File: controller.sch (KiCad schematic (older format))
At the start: 25 parts, among them J1 Conn_01x04, J2 Conn_01x08, J3 Conn_01x16, SW1 SW_Push, U1 PRTR5V0U2X, U2 AT90USB1286-AU, Y1 16MHz

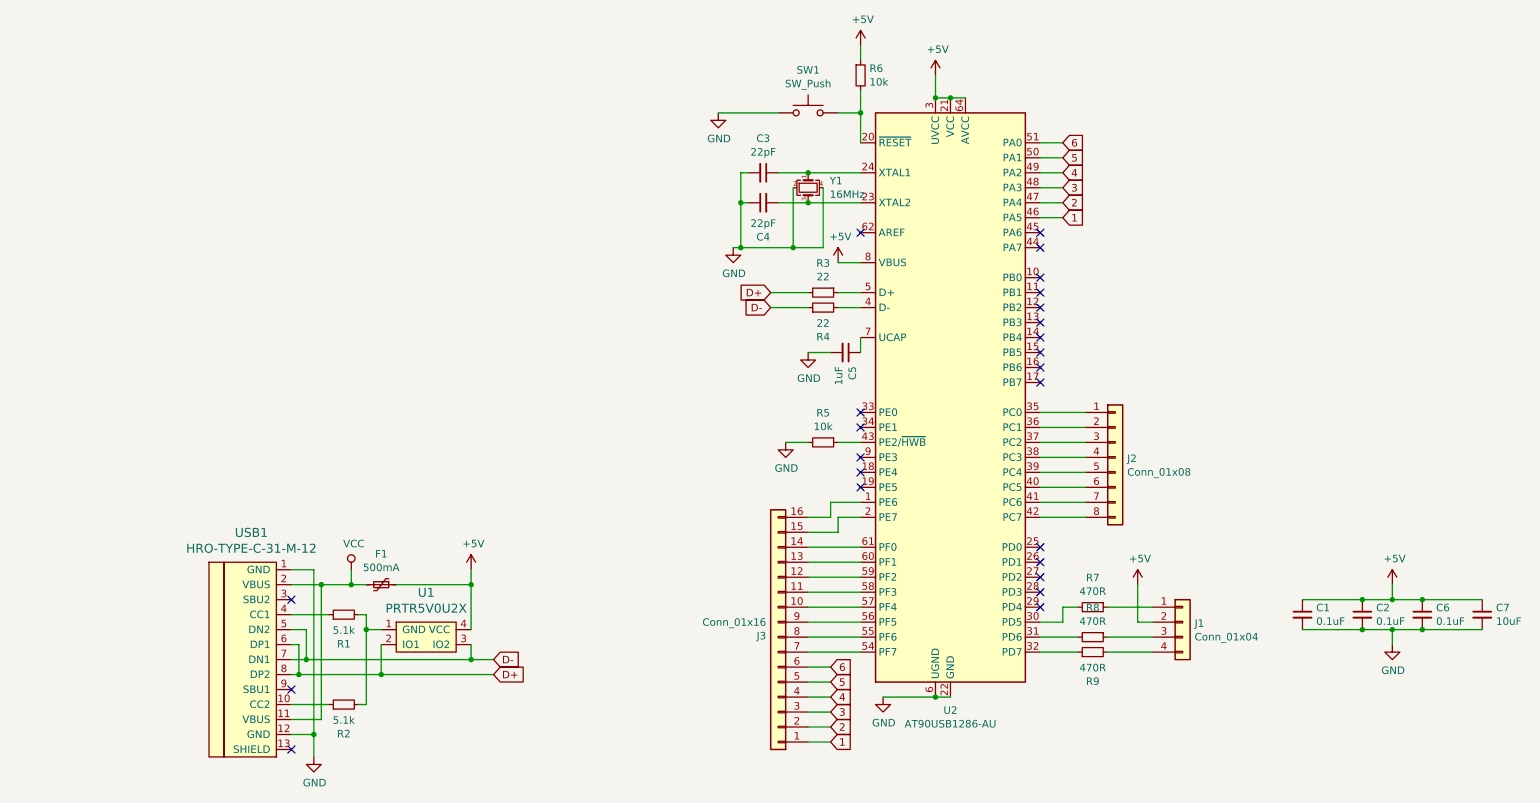
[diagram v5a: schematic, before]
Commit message: rev 2
Adjusted ucb-c location, fixed grounding error, changed some sizes to be more snug
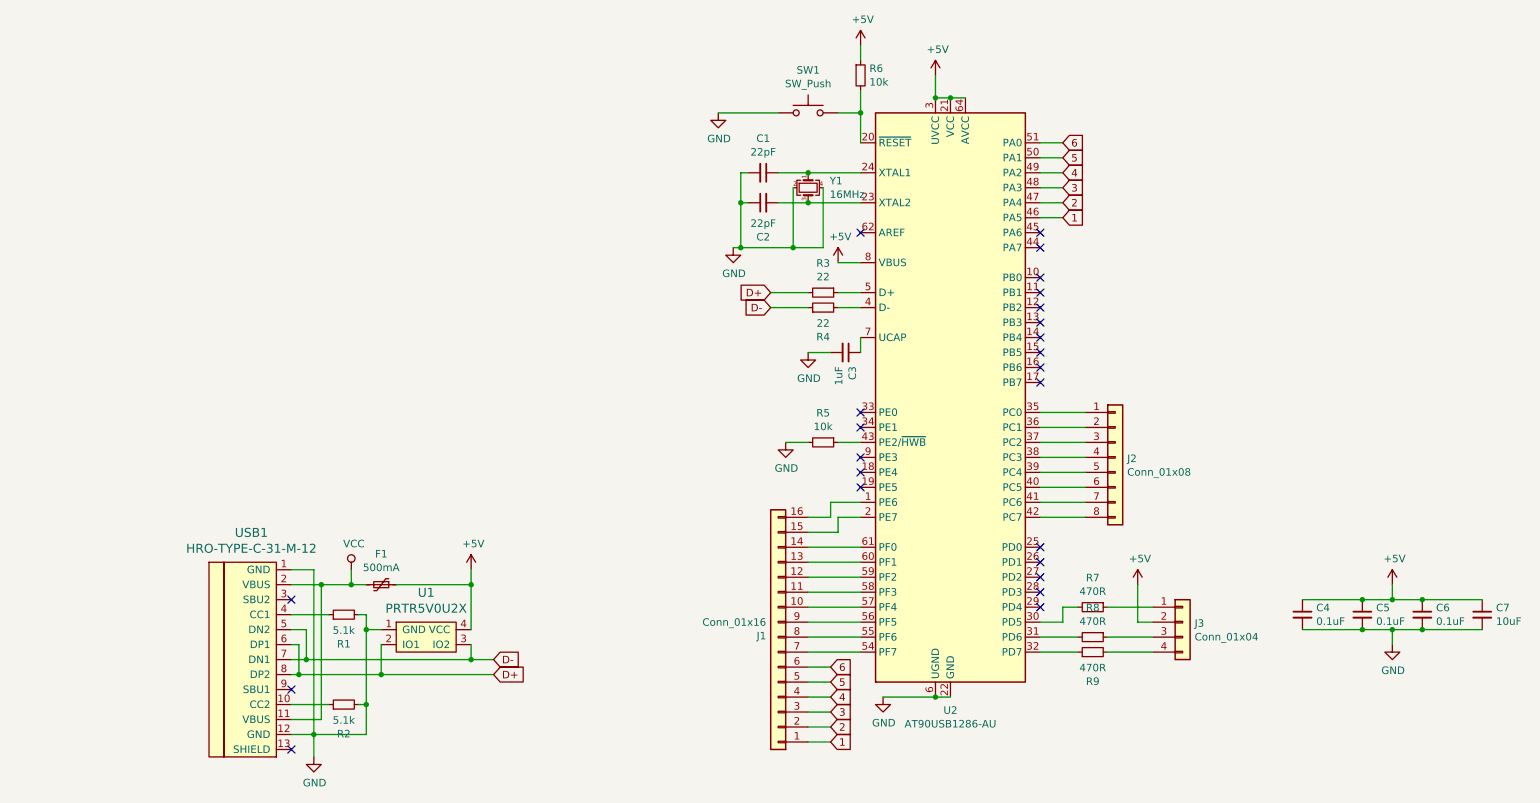
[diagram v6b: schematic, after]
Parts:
- renumbered C3 to C1, C4 to C2, C5 to C3, C1 to C4, C2 to C5, J3 to J1, J1 to J3
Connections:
- net GND: now also R1.2, R2.2, U1.1 (GND)
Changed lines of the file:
@@
 $EndDescr
 $Comp
-L Device:C_Small C1
+L Device:C_Small C4
 U 1 1 5DB8A8F2
 P 9100 4950
-F 0 "C1" H 9192 4996 50  0000 L CNN
+F 0 "C4" H 9192 4996 50  0000 L CNN
 F 1 "0.1uF" H 9192 4905 50  0000 L CNN
 F 2 "Capacitor_SMD:C_0805_2012Metric" H 9100 4950 50  0001 C CNN
@@
 $EndComp
 $Comp
-L Device:C_Small C2
+L Device:C_Small C5
 U 1 1 5DB8DED1
 P 9500 4950
-F 0 "C2" H 9592 4996 50  0000 L CNN
+F 0 "C5" H 9592 4996 50  0000 L CNN
 F 1 "0.1uF" H 9592 4905 50  0000 L CNN
 F 2 "Capacitor_SMD:C_0805_2012Metric" H 9500 4950 50  0001 C CNN
@@
 	9900 4850 9700 4850
 $Comp
-L power:GND #PWR0105
+L power:GND #PWR014
 U 1 1 5DB91595
 P 9700 5150
-F 0 "#PWR0105" H 9700 4900 50  0001 C CNN
+F 0 "#PWR014" H 9700 4900 50  0001 C CNN
 F 1 "GND" H 9705 4977 50  0000 C CNN
 F 2 "" H 9700 5150 50  0001 C CNN
@@
 	9700 5050 9900 5050
 $Comp
-L power:+5V #PWR0106
+L power:+5V #PWR013
 U 1 1 5DB91DDE
 P 9700 4750
-F 0 "#PWR0106" H 9700 4600 50  0001 C CNN
+F 0 "#PWR013" H 9700 4600 50  0001 C CNN
 F 1 "+5V" H 9715 4923 50  0000 C CNN
 F 2 "" H 9700 4750 50  0001 C CNN
@@
 $EndComp
 $Comp
-L power:GND #PWR0101
+L power:GND #PWR010
 U 1 1 5DC2B612
 P 6300 5500
-F 0 "#PWR0101" H 6300 5250 50  0001 C CNN
+F 0 "#PWR010" H 6300 5250 50  0001 C CNN
 F 1 "GND" H 6305 5327 50  0000 C CNN
 F 2 "" H 6300 5500 50  0001 C CNN
@@
 	6650 5500 6750 5500
 $Comp
-L Device:C_Small C5
+L Device:C_Small C3
 U 1 1 5DC407FB
 P 6050 3200
-F 0 "C5" H 6142 3246 50  0000 L CNN
+F 0 "C3" H 6142 3246 50  0000 L CNN
 F 1 "1uF" H 6142 3155 50  0000 L CNN
 F 2 "Capacitor_SMD:C_0805_2012Metric" H 6050 3200 50  0001 C CNN
@@
 $EndComp
 $Comp
-L power:GND #PWR0102
+L power:GND #PWR07
 U 1 1 5DC410EB
 P 5800 3200
-F 0 "#PWR0102" H 5800 2950 50  0001 C CNN
+F 0 "#PWR07" H 5800 2950 50  0001 C CNN
 F 1 "GND" H 5805 3027 50  0000 C CNN
 F 2 "" H 5800 3200 50  0001 C CNN
@@
 $EndComp
 $Comp
-L Device:C_Small C4
+L Device:C_Small C2
 U 1 1 5DC4A2A6
 P 5500 2200
-F 0 "C4" V 5271 2200 50  0000 C CNN
+F 0 "C2" V 5271 2200 50  0000 C CNN
 F 1 "22pF" V 5362 2200 50  0000 C CNN
 F 2 "Capacitor_SMD:C_0805_2012Metric" H 5500 2200 50  0001 C CNN
@@
 $EndComp
 $Comp
-L Device:C_Small C3
+L Device:C_Small C1
 U 1 1 5DC4A6AE
 P 5500 2000
-F 0 "C3" V 5271 2000 50  0000 C CNN
+F 0 "C1" V 5271 2000 50  0000 C CNN
 F 1 "22pF" V 5362 2000 50  0000 C CNN
 F 2 "Capacitor_SMD:C_0805_2012Metric" H 5500 2000 50  0001 C CNN
@@
 $EndComp
 $Comp
-L power:GND #PWR0103
+L power:GND #PWR05
 U 1 1 5DC4AACE
 P 5300 2500
-F 0 "#PWR0103" H 5300 2250 50  0001 C CNN
+F 0 "#PWR05" H 5300 2250 50  0001 C CNN
 F 1 "GND" H 5305 2327 50  0000 C CNN
 F 2 "" H 5300 2500 50  0001 C CNN
@@
 $EndComp
 $Comp
-L power:GND #PWR0104
+L power:GND #PWR04
 U 1 1 5DC7C02B
 P 5200 1600
-F 0 "#PWR0104" H 5200 1350 50  0001 C CNN
+F 0 "#PWR04" H 5200 1350 50  0001 C CNN
 F 1 "GND" H 5205 1427 50  0000 C CNN
 F 2 "" H 5200 1600 50  0001 C CNN
@@
 $EndComp
 $Comp
-L power:+5V #PWR0107
+L power:+5V #PWR09
 U 1 1 5DC832C4
 P 6150 1150
-F 0 "#PWR0107" H 6150 1000 50  0001 C CNN
+F 0 "#PWR09" H 6150 1000 50  0001 C CNN
 F 1 "+5V" H 6165 1323 50  0000 C CNN
 F 2 "" H 6150 1150 50  0001 C CNN
@@
 $EndComp
 $Comp
-L power:GND #PWR0108
+L power:GND #PWR06
 U 1 1 5DCA96CA
 P 5650 3800
-F 0 "#PWR0108" H 5650 3550 50  0001 C CNN
+F 0 "#PWR06" H 5650 3550 50  0001 C CNN
 F 1 "GND" H 5655 3627 50  0000 C CNN
 F 2 "" H 5650 3800 50  0001 C CNN
@@
 	6000 3800 6150 3800
 $Comp
-L power:+5V #PWR0109
+L power:+5V #PWR08
 U 1 1 5DCB1A24
 P 6000 2600
-F 0 "#PWR0109" H 6000 2450 50  0001 C CNN
+F 0 "#PWR08" H 6000 2450 50  0001 C CNN
 F 1 "+5V" H 6015 2773 50  0000 C CNN
 F 2 "" H 6000 2600 50  0001 C CNN
@@
 	6750 1500 6650 1500
 $Comp
-L power:+5V #PWR0110
+L power:+5V #PWR011
 U 1 1 5DCD1392
 P 6650 1350
-F 0 "#PWR0110" H 6650 1200 50  0001 C CNN
+F 0 "#PWR011" H 6650 1200 50  0001 C CNN
 F 1 "+5V" H 6665 1523 50  0000 C CNN
 F 2 "" H 6650 1350 50  0001 C CNN
@@
 Connection ~ 6650 1500
 $Comp
-L power:+5V #PWR0111
+L power:+5V #PWR012
 U 1 1 5DD3F67F
 P 8000 4750
-F 0 "#PWR0111" H 8000 4600 50  0001 C CNN
+F 0 "#PWR012" H 8000 4600 50  0001 C CNN
 F 1 "+5V" H 8015 4923 50  0000 C CNN
 F 2 "" H 8000 4750 50  0001 C CNN
@@
 Connection ~ 2500 5750
 $Comp
-L power:GND #PWR0112
+L power:GND #PWR01
 U 1 1 5DBE1745
 P 2500 5900
-F 0 "#PWR0112" H 2500 5650 50  0001 C CNN
+F 0 "#PWR01" H 2500 5650 50  0001 C CNN
 F 1 "GND" H 2505 5727 50  0000 C CNN
 F 2 "" H 2500 5900 50  0001 C CNN
@@
 	2350 4750 2550 4750
 $Comp
-L power:+5V #PWR0113
+L power:+5V #PWR03
 U 1 1 5DC0A05B
 P 3550 4650
-F 0 "#PWR0113" H 3550 4500 50  0001 C CNN
+F 0 "#PWR03" H 3550 4500 50  0001 C CNN
 F 1 "+5V" H 3565 4823 50  0000 C CNN
 F 2 "" H 3550 4650 50  0001 C CNN
@@
 $EndComp
 $Comp
-L power:VCC #PWR0114
+L power:VCC #PWR02
 U 1 1 5DC0AAF8
 P 2750 4650
-F 0 "#PWR0114" H 2750 4500 50  0001 C CNN
+F 0 "#PWR02" H 2750 4500 50  0001 C CNN
 F 1 "VCC" H 2767 4823 50  0000 C CNN
 F 2 "" H 2750 4650 50  0001 C CNN
@@
 $EndComp
 $Comp
-L Connector_Generic:Conn_01x16 J3
+L Connector_Generic:Conn_01x16 J1
 U 1 1 5DD0A31D
 P 5600 5100
-F 0 "J3" H 5680 5092 50  0000 L CNN
+F 0 "J1" H 5680 5092 50  0000 L CNN
 F 1 "Conn_01x16" H 5680 5001 50  0000 L CNN
 F 2 "Connector_PinHeader_2.54mm:PinHeader_1x16_P2.54mm_Vertical" H 5600 5100 50  0001 C CNN
@@
 $EndComp
 $Comp
-L Connector_Generic:Conn_01x04 J1
+L Connector_Generic:Conn_01x04 J3
 U 1 1 5DD0B4D3
 P 8300 5000
-F 0 "J1" H 8380 4992 50  0000 L CNN
+F 0 "J3" H 8380 4992 50  0000 L CNN
 F 1 "Conn_01x04" H 8380 4901 50  0000 L CNN
 F 2 "Connector_PinHeader_2.54mm:PinHeader_1x04_P2.54mm_Vertical" H 8300 5000 50  0001 C CNN
@@
 	0    1    1    0
 $EndComp
+Wire Wire Line
+	2500 5750 2850 5750
+Wire Wire Line
+	2850 5750 2850 5550
+Connection ~ 2850 5550
 $EndSCHEMATC

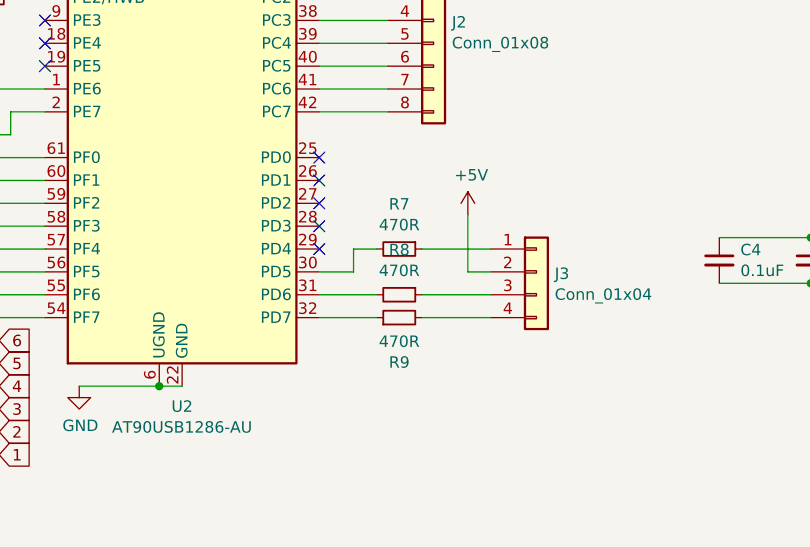
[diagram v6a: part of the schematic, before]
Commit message: fixed LED connector
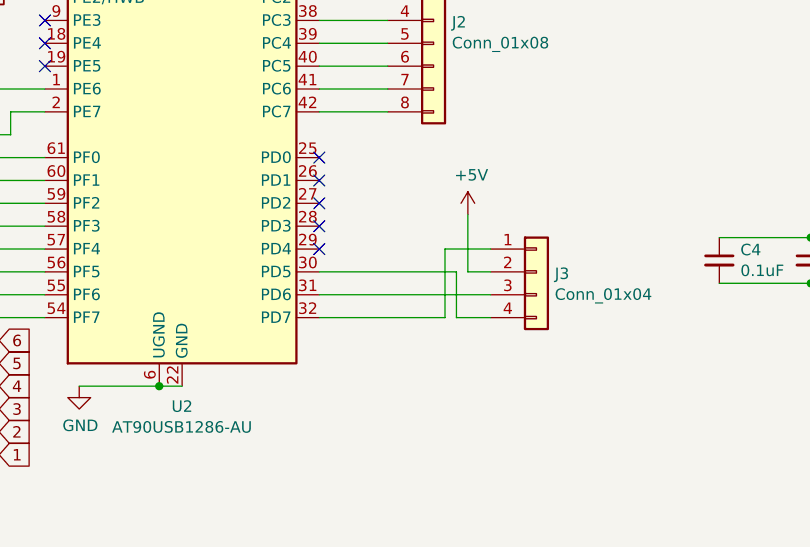
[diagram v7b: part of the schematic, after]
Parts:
- removed R7, R8, R9: 470R, Resistor_SMD:R_0805_2012Metric, symbol Device:R_Small
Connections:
- net at U2.30 (PD5): now also J3.4 (Pin_4)
- net at U2.31 (PD6): now also J3.3 (Pin_3)
- net at U2.32 (PD7): now also J3.1 (Pin_1)
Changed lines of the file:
@@
 	1    0    0    -1
 $EndComp
-Wire Wire Line
-	8100 5100 7800 5100
-Wire Wire Line
-	8100 5200 7800 5200
 NoConn ~ 6150 4100
 NoConn ~ 6150 4000
@@
 	1    0    0    -1
 $EndComp
-$Comp
-L Device:R_Small R7
-U 1 1 5DD1CC9E
-P 7700 4900
-F 0 "R7" V 7504 4900 50  0000 C CNN
-F 1 "470R" V 7595 4900 50  0000 C CNN
-F 2 "Resistor_SMD:R_0805_2012Metric" H 7700 4900 50  0001 C CNN
-F 3 "~" H 7700 4900 50  0001 C CNN
-	1    7700 4900
-	0    1    1    0
-$EndComp
-Wire Wire Line
-	7600 5100 7350 5100
-Wire Wire Line
-	7600 5200 7350 5200
 Wire Wire Line
 	8100 5000 8000 5000
 Wire Wire Line
 	8000 5000 8000 4750
-Wire Wire Line
-	8100 4900 7800 4900
-Wire Wire Line
-	7350 5000 7500 5000
-Wire Wire Line
-	7500 5000 7500 4900
-Wire Wire Line
-	7600 4900 7500 4900
-$Comp
-L Device:R_Small R9
-U 1 1 5DD64EB7
-P 7700 5200
-F 0 "R9" V 7504 5200 50  0000 C CNN
-F 1 "470R" V 7595 5200 50  0000 C CNN
-F 2 "Resistor_SMD:R_0805_2012Metric" H 7700 5200 50  0001 C CNN
-F 3 "~" H 7700 5200 50  0001 C CNN
-	1    7700 5200
-	0    -1   -1   0
-$EndComp
 Wire Wire Line
 	7350 3600 7650 3600
@@
 NoConn ~ 7350 2500
 NoConn ~ 7350 2400
-$Comp
-L Device:R_Small R8
-U 1 1 5DD1D4DA
-P 7700 5100
-F 0 "R8" V 7504 5100 50  0000 C CNN
-F 1 "470R" V 7595 5100 50  0000 C CNN
-F 2 "Resistor_SMD:R_0805_2012Metric" H 7700 5100 50  0001 C CNN
-F 3 "~" H 7700 5100 50  0001 C CNN
-	1    7700 5100
-	0    1    1    0
-$EndComp
 Wire Wire Line
 	2500 5750 2850 5750
@@
 	2850 5750 2850 5550
 Connection ~ 2850 5550
+Wire Wire Line
+	8100 5100 7350 5100
+Wire Wire Line
+	8100 5200 7950 5200
+Wire Wire Line
+	7950 5200 7950 5000
+Wire Wire Line
+	7950 5000 7350 5000
+Wire Wire Line
+	8100 4900 7900 4900
+Wire Wire Line
+	7900 4900 7900 5200
+Wire Wire Line
+	7900 5200 7350 5200
 $EndSCHEMATC
